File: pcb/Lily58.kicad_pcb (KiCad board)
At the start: 2 copper layers, 142.5 x 106.3 mm, 88 parts, among them J1 LED, J2 4PIN, P1 i2c_pin, P2 i2c_pin, P3 ICSP, SW1 SW_PUSH, SW10 SW_PUSH, SW11 SW_PUSH, SW12 SW_PUSH, SW13 SW_PUSH, SW14 SW_PUSH, SW15 SW_PUSH, SW16 SW_PUSH, SW17 SW_PUSH, SW18 SW_PUSH, SW19 SW_PUSH, SW2 SW_PUSH, SW20 SW_PUSH, SW21 SW_PUSH, SW22 SW_PUSH, SW23 SW_PUSH, SW24 SW_PUSH, SW25 SW_PUSH, SW26 SW_PUSH, SW27 SW_PUSH, SW28 SW_PUSH, SW29 SW_PUSH, SW3 SW_PUSH, SW4 SW_PUSH, SW5 SW_PUSH, SW6 SW_PUSH, SW7 SW_PUSH, SW8 SW_PUSH, SW9 SW_PUSH, U1 ProMicro

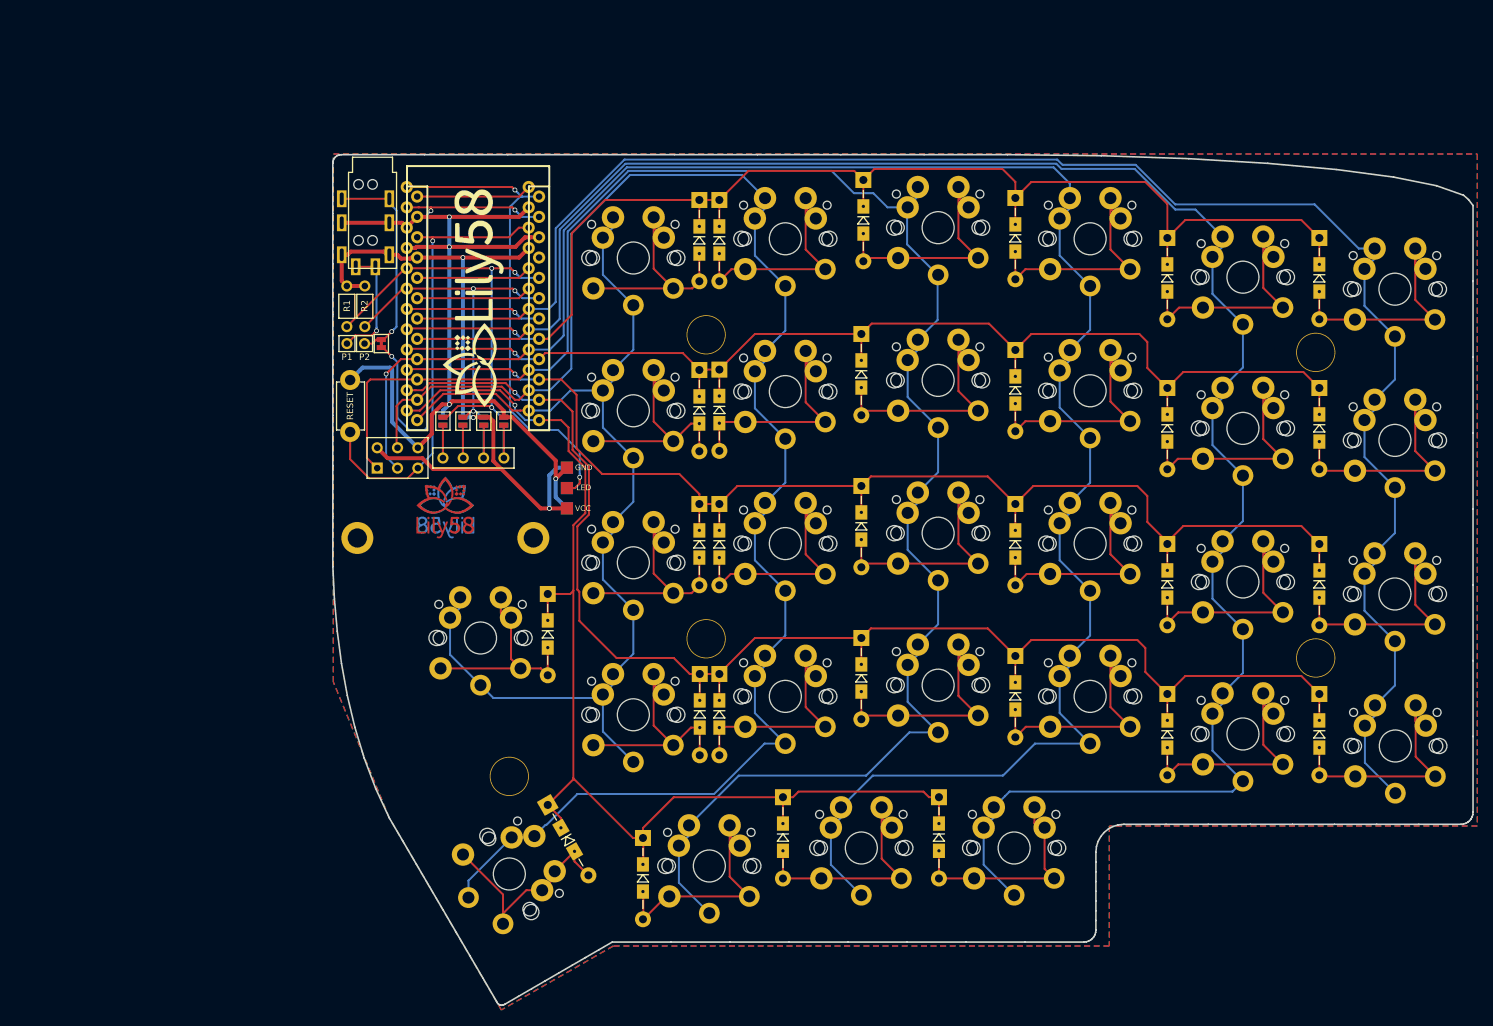
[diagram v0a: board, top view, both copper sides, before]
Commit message: Start of update to use my library and re-route
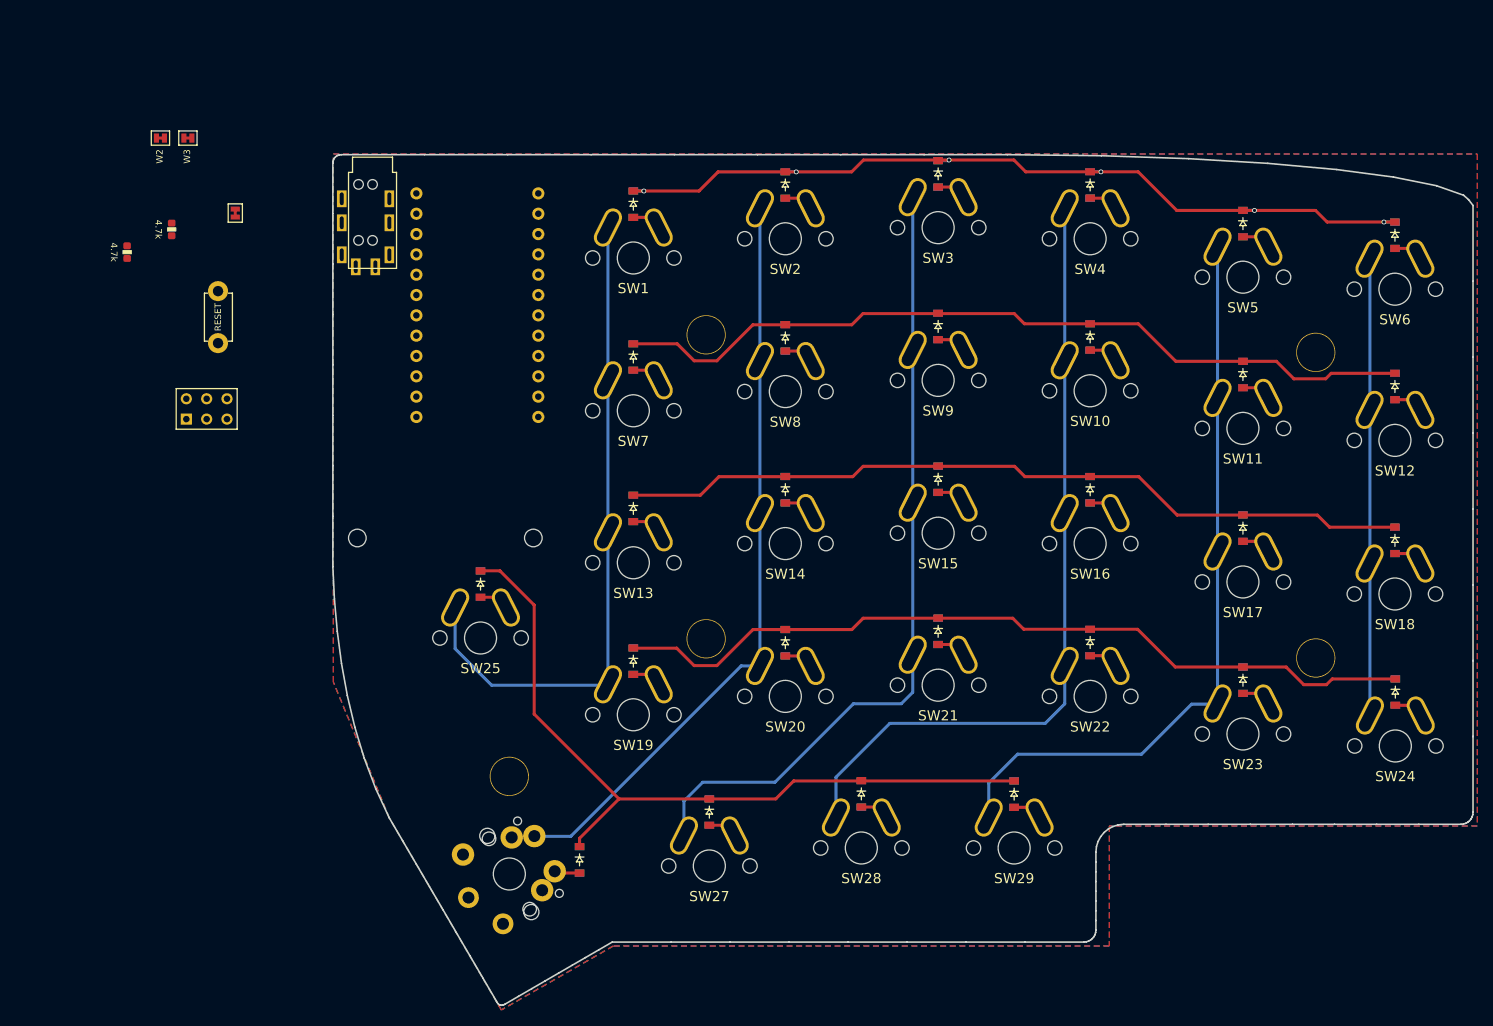
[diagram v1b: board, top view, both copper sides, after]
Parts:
- removed G*** (x2): LOGO, Lily58-footprint:lily58_logo_2
- removed G*** (x2): LOGO, Lily58-footprint:lily58_logo_3
- removed J1: LED, Lily58-footprint:StripLED
- removed JP1, JP2, JP3, JP4, JP5, JP6, JP7, JP8: , Lily58-footprint:Jumper
- removed OLED: OLED, Lily58-footprint:MY_SIL-4
- removed P1, P2: i2c_pin, Lily58-footprint:1pin_conn
- added W2: I2C_jmp_CLK, Lily58-footprint:jumper_data, F.Cu at (61.4, 35.0)
- added W3: I2C_jmp_SDA, Lily58-footprint:jumper_data, F.Cu at (64.8, 35.0)
- D1, D10, D11, D12, D13, D14, D15, D16, D17, D18, D19, D2, D20, D21, D22, D23, D24, D25, D26, D27, D28, D29, D3, D4, D5, D6, D7, D8, D9: footprint Lily58-footprint:Diode_TH_SOD123 -> Keyboard_Footprints:D_SOD-123
- R1, R2: value R -> 4.7k; footprint Lily58-footprint:RESISTOR_mini -> Keyboard_Footprints:R_0603
- SW1, SW10, SW11, SW12, SW13, SW14, SW15, SW16, SW17, SW18, SW19, SW2, SW20, SW21, SW22, SW23, SW24, SW25, SW27, SW28, SW29, SW3, SW4, SW5, SW6, SW7, SW8, SW9: footprint Lily58-footprint:MX_PG1350-Under_FLIP_HOLES_18mm -> Keyboard_Footprints:MX_1U
- TH1, TH2: footprint Lily58-footprint:M2_HOLE_PCB -> Lily58-footprint:HOLE_M2
- U1: footprint Lily58-footprint:ProMicro_rev2 -> Keyboard_Footprints:ProMicro_rev
- W1: value jumper -> RX_jmp
- moved R1 28.3 mm to (57.2, 49.3)
- moved R2 26.0 mm to (62.8, 46.4)
- moved P3 24.6 mm to (67.2, 68.9)
- moved W1 24.5 mm to (70.7, 44.4)
- moved RSW1 19.9 mm to (68.6, 57.4)
- moved D8 12.2 mm to (139.5, 60.0)
- moved D20 12.1 mm to (139.5, 98.1)
- moved D17 11.7 mm to (196.7, 83.8)
- moved D27 11.7 mm to (130.0, 119.3)
- moved D5 11.6 mm to (196.7, 45.7)
- moved D23 11.6 mm to (196.7, 102.8)
- moved D11 11.6 mm to (196.7, 64.6)
- moved D16 11.6 mm to (177.6, 79.0)
- moved D22 11.5 mm to (177.6, 98.1)
- moved D4 11.5 mm to (177.6, 40.9)
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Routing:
- net col0: track 217.9 -> 57.1 mm
- net col1: track 245.7 -> 94.1 mm
- net col2: track 246.8 -> 99.4 mm, vias 1 -> 0
- net col3: track 229.7 -> 100.4 mm
- net GND: track 117.4 -> 0.00 mm, vias 4 -> 0
- net col4: track 204.8 -> 94.3 mm
- net VCC: track 94.8 -> 0.00 mm, vias 3 -> 0
- net row3: track 176.5 -> 102.4 mm, vias 1 -> 0
- net LED: track 63.8 -> 0.00 mm, vias 2 -> 0
- net DATA: track 59.0 -> 0.00 mm, vias 3 -> 0
- net RESET: track 57.5 -> 0.00 mm, vias 1 -> 0
- net row2: track 155.9 -> 99.8 mm, vias 1 -> 0
- net SDA: track 53.7 -> 0.00 mm, vias 3 -> 0
- net row0: track 160.9 -> 108.3 mm, vias 1 -> 6
- net col5: track 135.9 -> 83.3 mm
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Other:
- board text removed: "GND"
- board text removed: "LED"
- board text removed: "VCC"

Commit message: Update comps
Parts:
- added REF**: PJ-320A, Keyboard_Footprints:PJ-320A, B.Cu at (68.6, 22.4)
- added REF**: PJ-320A, Keyboard_Footprints:PJ-320A, F.Cu at (76.5, 22.4)
- added REF**: CUI_sj_43515RS, Keyboard_Footprints:CUI_sj_43515RS, F.Cu at (48.4, 31.8)
- moved P3 30.7 mm to (95.7, 80.4), turned to 270 degrees
- moved W3 11.8 mm to (73.6, 42.8), turned to 90 degrees
- moved W2 11.4 mm to (69.9, 42.6), turned to 90 degrees
- moved W1 10.2 mm to (60.7, 42.6)
- moved R2 10.0 mm to (68.7, 54.6)
- moved RSW1 9.01 mm to (63.9, 65.1)
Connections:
- net LED renamed Net-(U1-Pad1)
- net Net-(J2-Pad3) renamed /sp_data
- net Net-(J2-Pad4) renamed /sp_clk
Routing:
- net col0: track 57.1 -> 179.8 mm, vias 0 -> 2
- net col1: track 94.1 -> 198.1 mm, vias 0 -> 2
- net col2: track 99.4 -> 196.1 mm, vias 0 -> 2
- net col3: track 100.4 -> 176.1 mm, vias 0 -> 2
- net col4: track 94.3 -> 160.9 mm, vias 0 -> 2
- net row3: track 102.4 -> 167.0 mm, vias 0 -> 8
- net row2: track 99.8 -> 148.7 mm, vias 0 -> 8
- net row4: track 95.4 -> 135.6 mm, vias 0 -> 6
- net row0: track 108.3 -> 146.0 mm, vias 6 -> 7
- net row1: track 102.2 -> 137.3 mm, vias 0 -> 8
- net col5: track 83.3 -> 107.4 mm, vias 0 -> 1
- net Net-(D26-Pad2): track 2.98 -> 26.7 mm
- net DATA: track 0.00 -> 11.4 mm, vias 0 -> 1
- net SDA: track 0.00 -> 11.3 mm, vias 0 -> 1
- net SCL: track 0.00 -> 11.2 mm, vias 0 -> 1
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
